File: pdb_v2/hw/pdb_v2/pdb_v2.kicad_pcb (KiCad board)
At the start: 4 copper layers, 82.1 x 66.3 mm, 75 parts, among them J1 XT30-M_Ver, J2 JST-PH_01x02, J3 Conn_01x06_Pin, J5 JST-PH_01x02, J6 Conn_01x03, J7 Conn_01x03, J8 Conn_01x04, Q1 60Vds, SW1 SW_Push, SW2 SW_Push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

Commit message: improved
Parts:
- removed the H1 at (2.77, 2.77)
- removed the H2 at (2.77, 9.32)
- SW1, SW2: footprint Button_Switch_SMD:SW_SPST_TL3342 -> Button_Switch_THT:SW_PUSH_6mm
- moved D5 31.9 mm to (62.0, 58.2), turned to 180 degrees
- moved R9 30.4 mm to (62.0, 59.9), turned to 180 degrees
- moved G*** 29.3 mm to (53.2, 35.2)
- moved SW1 22.4 mm to (49.6, 65.3), turned to 0 degrees
- moved SW2 4.21 mm to (56.1, 61.0), turned to 180 degrees
- moved J6 2.81 mm to (87.0, 47.9)
- moved J7 2.81 mm to (87.0, 56.8)
- moved H2 2.04 mm to (89.0, 15.1)
- moved D6 1.99 mm to (62.0, 63.1)
- moved R3 1.82 mm to (86.9, 65.7)
- moved C16 1.80 mm to (86.8, 69.0)
- moved J8 1.34 mm to (33.8, 62.8)
- moved R10 1.31 mm to (62.0, 61.5)
- moved C5 1.24 mm to (84.3, 66.5), turned to 90 degrees
- moved L3 1.16 mm to (73.8, 40.3)
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- renumbered H3 to H1, H4 to H2
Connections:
- R9 pad 1: 3V3_BUS -> /LED
- U2 pad 30: unconnected-(U2-IO18-Pad30) -> /LED
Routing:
- net /EN: track 122.1 -> 70.8 mm, vias 2 -> 0
- net 12V_BUS: track 148.3 -> 124.3 mm
- net 3V3_BUS: track 165.1 -> 146.7 mm
- net GND: track 167.5 -> 174.2 mm, vias 75 -> 73
- net /BOOT: track 60.7 -> 55.6 mm, vias 1 -> 0
- net /BMS RX: track 27.7 -> 24.8 mm
- net /VESC TX: track 7.84 -> 4.93 mm
- net /BMS TX: track 29.0 -> 26.1 mm
- net /RX: track 45.8 -> 48.6 mm, vias 0 -> 2
- net /VESC RX: track 7.54 -> 4.89 mm
- net /TX: track 47.5 -> 50.1 mm, vias 1 -> 2
- net /LED: track 0.00 -> 1.89 mm
- net Net-(U2-IO19): track 3.39 -> 2.02 mm
- net /OLED SCL: track 38.3 -> 39.6 mm
- net /OLED SDA: track 35.1 -> 36.4 mm
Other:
- board size 82.1 x 66.3 mm -> 80.1 x 66.3 mm

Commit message: Still relabeling
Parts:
- moved J3 1.55 mm to (18.1, 55.9)
- moved SW2 1.30 mm to (56.1, 59.8)
- moved J6 1.05 mm to (87.5, 46.9)
- moved J7 0.54 mm to (87.5, 56.5)
- moved SW1 0.15 mm to (49.6, 65.2)
- moved C6 0.12 mm to (62.1, 54.5)
- moved D5 0.12 mm to (62.0, 58.1)
- moved D6 0.12 mm to (62.0, 63.0)
- moved R10 0.12 mm to (62.0, 61.4)
- moved R9 0.12 mm to (62.0, 59.8)
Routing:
- net GND: track 174.2 -> 177.1 mm
- net /OLED SCL: track 39.6 -> 37.5 mm
- net /BMS TX: track 26.1 -> 27.9 mm
- net /BMS RX: track 24.8 -> 25.6 mm
- net /EN: track 70.8 -> 71.5 mm
- net /RX: track 48.6 -> 49.2 mm, vias 2 -> 0
- net /VESC TX: track 4.93 -> 5.51 mm
- net /TX: track 50.1 -> 50.6 mm
- net /VESC RX: track 4.89 -> 5.43 mm
- net /OLED SDA: track 36.4 -> 36.0 mm, vias 0 -> 2
- net /BOOT: track 55.6 -> 55.3 mm, vias 0 -> 2
- added copper zone on In2.Cu, net GND
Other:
- board text added: "Power Distribution + Telemetry"

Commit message: Sent to Matthew for review
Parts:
- removed the G*** at (53.2, 35.2)
- added G***: LOGO, LOGO, F.Cu at (14.8, 40.6)
- added G***: LOGO, LOGO, F.Cu at (54.3, 37.5)
- moved GND1 21.6 mm to (15.6, 16.1)
- moved G*** 7.50 mm to (51.8, 34.2)
- moved FB_3V3 3.29 mm to (63.8, 37.6)
- moved VBAT1 3.18 mm to (15.6, 27.0)
- moved EN_12V1 1.26 mm to (15.6, 21.4)
- moved J1 1.20 mm to (23.4, 35.9)
- moved 12V1 0.40 mm to (47.4, 28.3)
- moved GND2 0.40 mm to (53.4, 28.3)
- moved SW_12V1 0.40 mm to (38.3, 28.3)
- moved 3V3 0.06 mm to (88.0, 36.5)
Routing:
- net GND: track 177.1 -> 207.3 mm, vias 73 -> 81
- net Net-(U1-EN): track 21.6 -> 20.6 mm
- net VBAT: track 68.3 -> 69.1 mm
- net Net-(J1-Pin_2): track 5.33 -> 4.73 mm
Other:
- board text added: "BMS"
- board text added: "F25 Skateboard Power Distribution & Telemetry v2"
- board text added: "Power Distribution & Telemetry Board v2 for F25 Skateboard by Leopoldo Mendoza, Mike Yao, Arnav Shah"
- board text added: "VESC"
- board text removed: "Power Distribution + Telemetry"
- board text removed: "Power Distribution + Telemetry Board v2 for F25 Skateboard by Leopoldo Mendoza, Mike Yao, Arnav Shah"

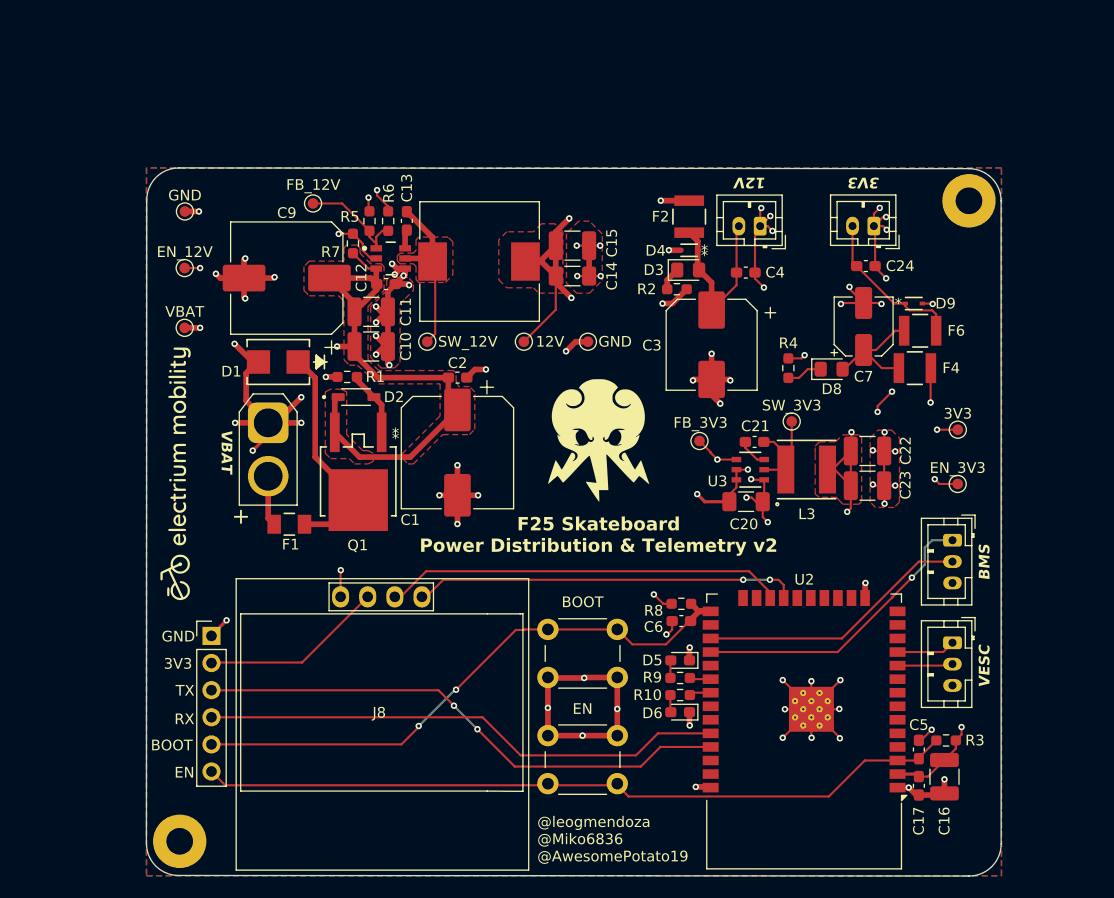
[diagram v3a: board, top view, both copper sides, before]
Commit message: Add stitching vias
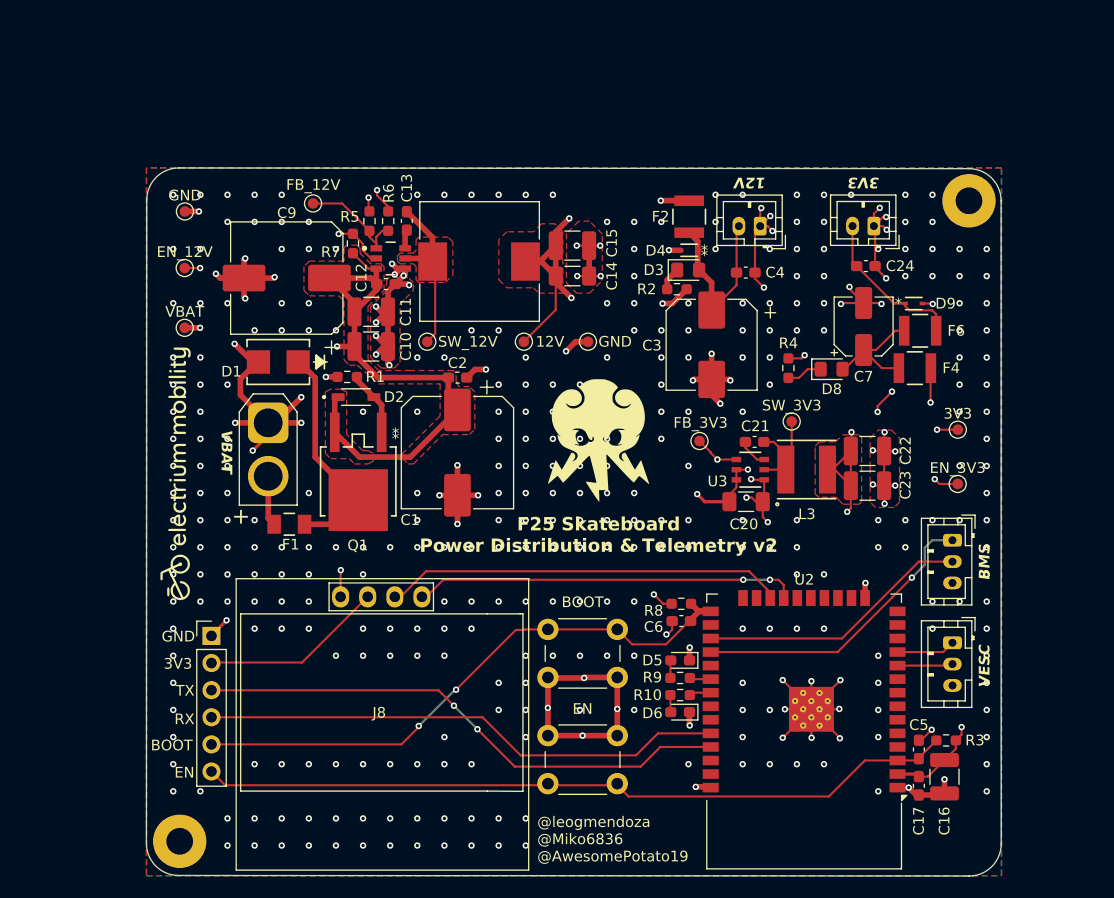
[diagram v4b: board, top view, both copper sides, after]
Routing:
- net GND: track 207.3 -> 207.7 mm, vias 81 -> 399

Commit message: Zipped up gerber + drill files!
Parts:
- removed GND2: GND, test_point_custom:TestPoint_Pad_D1.0mm
- moved G*** 6.46 mm to (52.1, 40.6)
- moved 12V1 4.55 mm to (51.9, 28.2)
- moved SW_12V1 1.90 mm to (40.2, 28.3)
- moved FB_3V3 0.46 mm to (63.5, 37.2)
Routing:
- net GND: track 207.7 -> 112.5 mm, vias 399 -> 118
- net /TX: track 50.6 -> 51.8 mm
- net /BOOT: track 55.3 -> 56.5 mm
- net 12V_BUS: track 124.7 -> 124.0 mm
- net Net-(U1-SW): track 16.1 -> 16.7 mm
